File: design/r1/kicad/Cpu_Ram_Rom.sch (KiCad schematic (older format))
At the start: 13 parts, among them IC1 MC68010P10, U1 AT28C64B-15PU, U2 AT28C64B-15PU, U3 AS6C4008-55PCN, U4 AS6C4008-55PCN

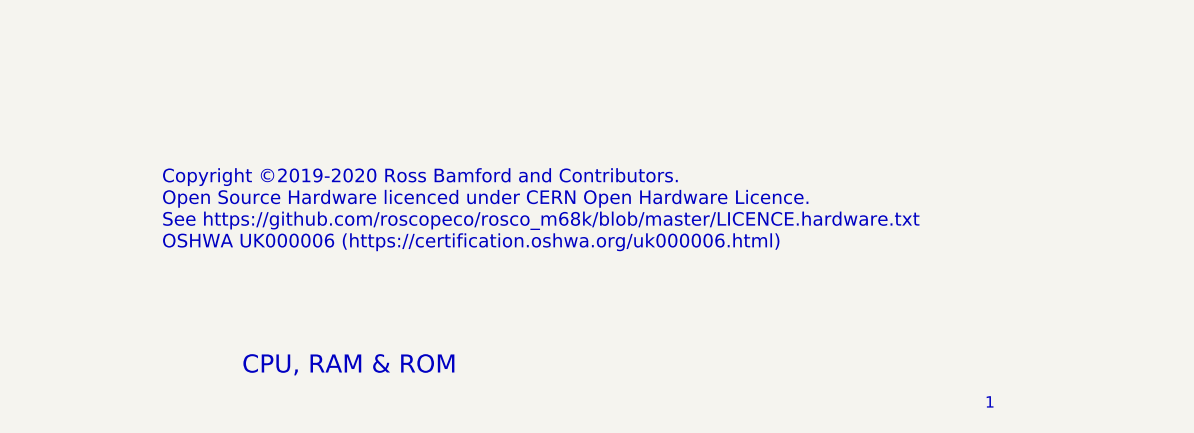
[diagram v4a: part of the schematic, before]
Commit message: Fix #18 and apply suggestions from #17
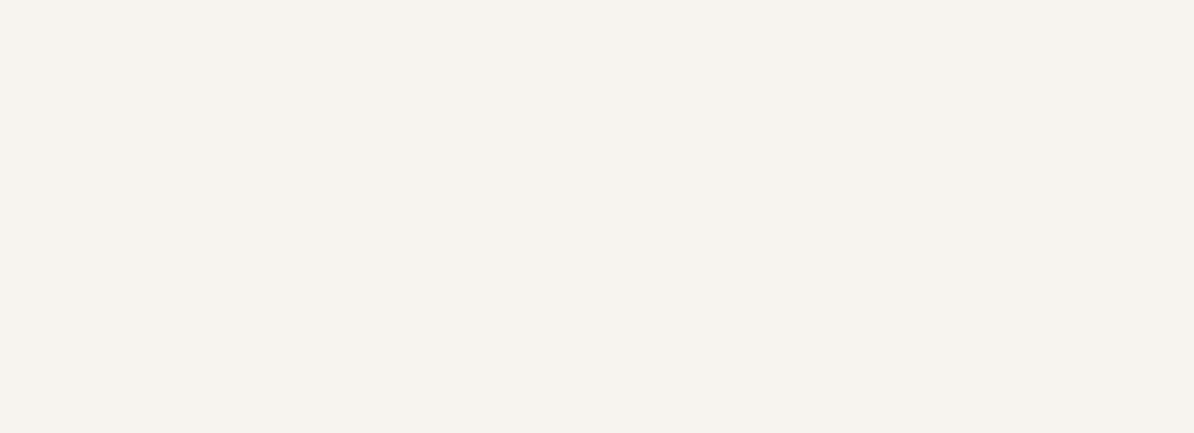
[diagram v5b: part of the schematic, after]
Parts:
- U1, U2: footprint (none) -> rosco_m68k:DIP254P1524X482-28
- U3, U4: footprint (none) -> rosco_m68k:DIP254P1524X393-32
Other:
- note removed: "1"
- note removed: "CPU, RAM & ROM"
- note removed: "Copyright ©2019-2020 Ross Bamford and Contributors.\nOpen Source Hardware licenced under CERN Open Hardware Licence. \nSee https://github.com/roscopeco/rosco_m68k/blob/master/LICENCE.hardware.txt\nOSHWA UK000006 (https://certification.oshwa.org/uk000006.html)\n"
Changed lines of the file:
@@
 encoding utf-8
 Sheet 2 6
-Title ""
+Title "CPU, RAM & ROM"
 Date "2020-02-25"
-Rev ""
+Rev "1"
 Comp ""
-Comment1 ""
-Comment2 ""
-Comment3 ""
-Comment4 ""
+Comment1 "OSHWA UK000006 (https://certification.oshwa.org/uk000006.html)"
+Comment2 "See https://github.com/roscopeco/rosco_m68k/blob/master/LICENCE.hardware.txt"
+Comment3 "Open Source Hardware licenced under CERN Open Hardware Licence"
+Comment4 "Copyright 2019-2020 Ross Bamford and Contributors"
 $EndDescr
 Wire Wire Line
@@
 Wire Wire Line
 	8950 4250 9750 4250
-Text Notes 19800 10900 0    50   ~ 0
-1
-Text Notes 16550 10750 0    79   ~ 0
-CPU, RAM & ROM
-Text Notes 16200 10200 0    59   ~ 0
-Copyright ©2019-2020 Ross Bamford and Contributors.\nOpen Source Hardware licenced under CERN Open Hardware Licence. \nSee https://github.com/roscopeco/rosco_m68k/blob/master/LICENCE.hardware.txt\nOSHWA UK000006 (https://certification.oshwa.org/uk000006.html)\n
 $Comp
 L power:VCC #PWR0103
@@
 F 0 "U3" H 18250 5258 69  0000 C CNN
 F 1 "AS6C4008-55PCN" H 18250 5138 69  0000 C CNN
-F 2 "" H 18250 3650 50  0001 C CNN
+F 2 "rosco_m68k:DIP254P1524X393-32" H 18250 3650 50  0001 C CNN
 F 3 "" H 18250 3650 50  0001 C CNN
 	1    18250 3650
@@
 F 0 "U4" H 18250 8958 69  0000 C CNN
 F 1 "AS6C4008-55PCN" H 18250 8838 69  0000 C CNN
-F 2 "" H 18250 7350 50  0001 C CNN
+F 2 "rosco_m68k:DIP254P1524X393-32" H 18250 7350 50  0001 C CNN
 F 3 "" H 18250 7350 50  0001 C CNN
 	1    18250 7350
@@
 F 0 "U1" H 10450 4858 69  0000 C CNN
 F 1 "AT28C64B-15PU" H 10450 4738 69  0000 C CNN
-F 2 "" H 10450 3450 50  0001 C CNN
+F 2 "rosco_m68k:DIP254P1524X482-28" H 10450 3450 50  0001 C CNN
 F 3 "" H 10450 3450 50  0001 C CNN
 	1    10450 3450
@@
 F 0 "U2" H 10450 8558 69  0000 C CNN
 F 1 "AT28C64B-15PU" H 10450 8438 69  0000 C CNN
-F 2 "" H 10450 7150 50  0001 C CNN
+F 2 "rosco_m68k:DIP254P1524X482-28" H 10450 7150 50  0001 C CNN
 F 3 "" H 10450 7150 50  0001 C CNN
 	1    10450 7150
